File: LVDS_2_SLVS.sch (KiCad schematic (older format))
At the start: 6 parts

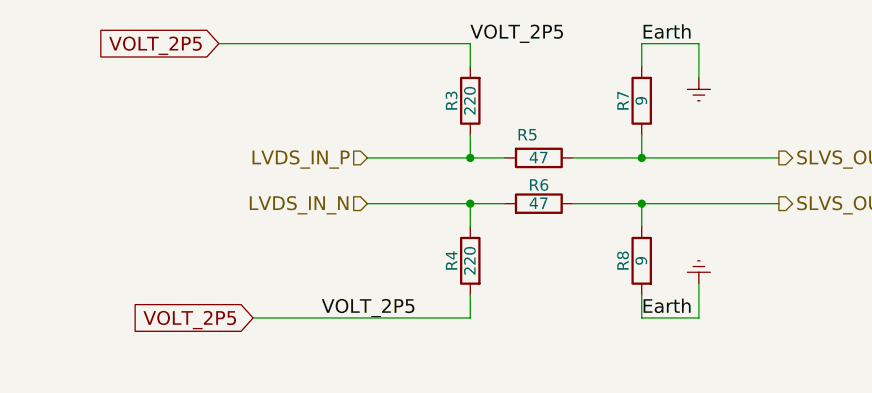
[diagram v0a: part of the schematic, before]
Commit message: Good, before replacing the swithches to TI ones
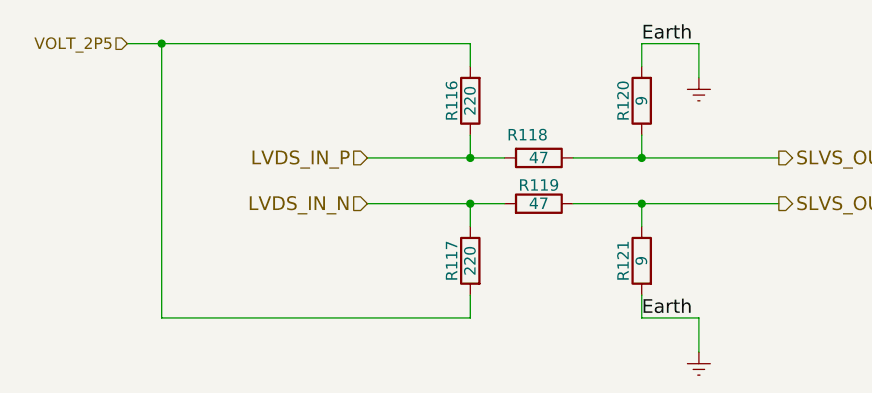
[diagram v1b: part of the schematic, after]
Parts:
- renumbered R6 to R100, R7 to R101, R8 to R102, R3 to R97, R4 to R98, R5 to R99

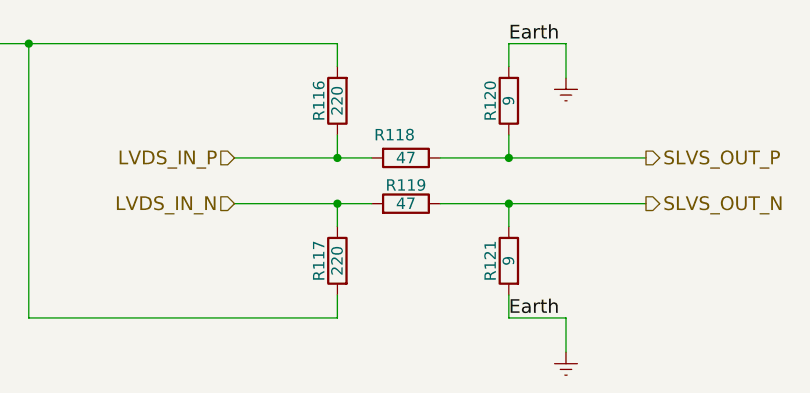
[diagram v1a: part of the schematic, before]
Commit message: good, added re-driver
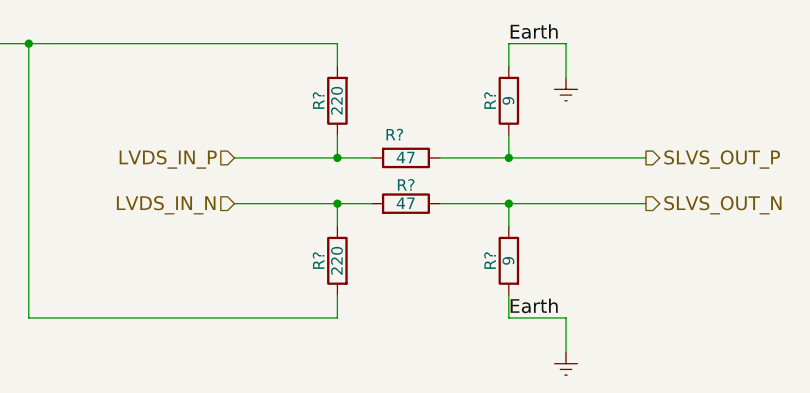
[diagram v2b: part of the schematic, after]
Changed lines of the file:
@@
 $Descr A4 11693 8268
 encoding utf-8
-Sheet 31 32
+Sheet 31 20
 Title ""
 Date ""
@@
 AR Path="/6191D89C/61A38142/61C10965/61958BD7/5955E861" Ref="R?"  Part="1"
 AR Path="/6191D89C/61A38142/61C10965/61946DF5/5955E861" Ref="R?"  Part="1"
-F 0 "R116" V 2680 1250 50  0000 C CNN
+AR Path="/6191D89C/61A814B9/61AF86EB/5955E861" Ref="R?"  Part="1"
+AR Path="/6191D89C/61A814B9/61AF8785/5955E861" Ref="R?"  Part="1"
+AR Path="/6191D89C/61A814B9/61AF878C/5955E861" Ref="R?"  Part="1"
+AR Path="/6191D89C/61A38142/61AF86EB/5955E861" Ref="R?"  Part="1"
+AR Path="/6191D89C/61A38142/61AF8785/5955E861" Ref="R?"  Part="1"
+AR Path="/6191D89C/61A38142/61AF878C/5955E861" Ref="R?"  Part="1"
+F 0 "R?" V 2680 1250 50  0000 C CNN
 F 1 "220" V 2600 1250 50  0000 C CNN
 F 2 "Resistors_SMD:R_0805" V 2530 1250 50  0001 C CNN
@@
 AR Path="/6191D89C/61A38142/61C10965/61958BD7/5955E8CA" Ref="R?"  Part="1"
 AR Path="/6191D89C/61A38142/61C10965/61946DF5/5955E8CA" Ref="R?"  Part="1"
-F 0 "R118" V 2800 1450 50  0000 C CNN
+AR Path="/6191D89C/61A814B9/61AF86EB/5955E8CA" Ref="R?"  Part="1"
+AR Path="/6191D89C/61A814B9/61AF8785/5955E8CA" Ref="R?"  Part="1"
+AR Path="/6191D89C/61A814B9/61AF878C/5955E8CA" Ref="R?"  Part="1"
+AR Path="/6191D89C/61A38142/61AF86EB/5955E8CA" Ref="R?"  Part="1"
+AR Path="/6191D89C/61A38142/61AF8785/5955E8CA" Ref="R?"  Part="1"
+AR Path="/6191D89C/61A38142/61AF878C/5955E8CA" Ref="R?"  Part="1"
+F 0 "R?" V 2800 1450 50  0000 C CNN
 F 1 "47" V 2900 1500 50  0000 C CNN
 F 2 "Resistors_SMD:R_0805" V 2830 1500 50  0001 C CNN
@@
 AR Path="/6191D89C/61A38142/61C10965/61958BD7/5955E920" Ref="R?"  Part="1"
 AR Path="/6191D89C/61A38142/61C10965/61946DF5/5955E920" Ref="R?"  Part="1"
-F 0 "R120" V 3430 1250 50  0000 C CNN
+AR Path="/6191D89C/61A814B9/61AF86EB/5955E920" Ref="R?"  Part="1"
+AR Path="/6191D89C/61A814B9/61AF8785/5955E920" Ref="R?"  Part="1"
+AR Path="/6191D89C/61A814B9/61AF878C/5955E920" Ref="R?"  Part="1"
+AR Path="/6191D89C/61A38142/61AF86EB/5955E920" Ref="R?"  Part="1"
+AR Path="/6191D89C/61A38142/61AF8785/5955E920" Ref="R?"  Part="1"
+AR Path="/6191D89C/61A38142/61AF878C/5955E920" Ref="R?"  Part="1"
+F 0 "R?" V 3430 1250 50  0000 C CNN
 F 1 "9" V 3350 1250 50  0000 C CNN
 F 2 "Resistors_SMD:R_0805" V 3280 1250 50  0001 C CNN
@@
 AR Path="/6191D89C/61A38142/61C10965/61958BD7/5955F5BB" Ref="R?"  Part="1"
 AR Path="/6191D89C/61A38142/61C10965/61946DF5/5955F5BB" Ref="R?"  Part="1"
-F 0 "R117" V 2680 1950 50  0000 C CNN
+AR Path="/6191D89C/61A814B9/61AF86EB/5955F5BB" Ref="R?"  Part="1"
+AR Path="/6191D89C/61A814B9/61AF8785/5955F5BB" Ref="R?"  Part="1"
+AR Path="/6191D89C/61A814B9/61AF878C/5955F5BB" Ref="R?"  Part="1"
+AR Path="/6191D89C/61A38142/61AF86EB/5955F5BB" Ref="R?"  Part="1"
+AR Path="/6191D89C/61A38142/61AF8785/5955F5BB" Ref="R?"  Part="1"
+AR Path="/6191D89C/61A38142/61AF878C/5955F5BB" Ref="R?"  Part="1"
+F 0 "R?" V 2680 1950 50  0000 C CNN
 F 1 "220" V 2600 1950 50  0000 C CNN
 F 2 "Resistors_SMD:R_0805" V 2530 1950 50  0001 C CNN
@@
 AR Path="/6191D89C/61A38142/61C10965/61958BD7/5955F5C4" Ref="R?"  Part="1"
 AR Path="/6191D89C/61A38142/61C10965/61946DF5/5955F5C4" Ref="R?"  Part="1"
-F 0 "R119" V 2980 1700 50  0000 C CNN
+AR Path="/6191D89C/61A814B9/61AF86EB/5955F5C4" Ref="R?"  Part="1"
+AR Path="/6191D89C/61A814B9/61AF8785/5955F5C4" Ref="R?"  Part="1"
+AR Path="/6191D89C/61A814B9/61AF878C/5955F5C4" Ref="R?"  Part="1"
+AR Path="/6191D89C/61A38142/61AF86EB/5955F5C4" Ref="R?"  Part="1"
+AR Path="/6191D89C/61A38142/61AF8785/5955F5C4" Ref="R?"  Part="1"
+AR Path="/6191D89C/61A38142/61AF878C/5955F5C4" Ref="R?"  Part="1"
+F 0 "R?" V 2980 1700 50  0000 C CNN
 F 1 "47" V 2900 1700 50  0000 C CNN
 F 2 "Resistors_SMD:R_0805" V 2830 1700 50  0001 C CNN
@@
 AR Path="/6191D89C/61A38142/61C10965/61958BD7/5955F5CD" Ref="R?"  Part="1"
 AR Path="/6191D89C/61A38142/61C10965/61946DF5/5955F5CD" Ref="R?"  Part="1"
-F 0 "R121" V 3430 1950 50  0000 C CNN
+AR Path="/6191D89C/61A814B9/61AF86EB/5955F5CD" Ref="R?"  Part="1"
+AR Path="/6191D89C/61A814B9/61AF8785/5955F5CD" Ref="R?"  Part="1"
+AR Path="/6191D89C/61A814B9/61AF878C/5955F5CD" Ref="R?"  Part="1"
+AR Path="/6191D89C/61A38142/61AF86EB/5955F5CD" Ref="R?"  Part="1"
+AR Path="/6191D89C/61A38142/61AF8785/5955F5CD" Ref="R?"  Part="1"
+AR Path="/6191D89C/61A38142/61AF878C/5955F5CD" Ref="R?"  Part="1"
+F 0 "R?" V 3430 1950 50  0000 C CNN
 F 1 "9" V 3350 1950 50  0000 C CNN
 F 2 "Resistors_SMD:R_0805" V 3280 1950 50  0001 C CNN
@@
 AR Path="/6191D89C/61A38142/61C10965/61958BD7/5955F5D7" Ref="#PWR?"  Part="1"
 AR Path="/6191D89C/61A38142/61C10965/61946DF5/5955F5D7" Ref="#PWR?"  Part="1"
-F 0 "#PWR077" H 3600 2100 50  0001 C CNN
+AR Path="/6191D89C/61A814B9/61AF86EB/5955F5D7" Ref="#PWR?"  Part="1"
+AR Path="/6191D89C/61A814B9/61AF8785/5955F5D7" Ref="#PWR?"  Part="1"
+AR Path="/6191D89C/61A814B9/61AF878C/5955F5D7" Ref="#PWR?"  Part="1"
+AR Path="/6191D89C/61A38142/61AF86EB/5955F5D7" Ref="#PWR?"  Part="1"
+AR Path="/6191D89C/61A38142/61AF8785/5955F5D7" Ref="#PWR?"  Part="1"
+AR Path="/6191D89C/61A38142/61AF878C/5955F5D7" Ref="#PWR?"  Part="1"
+F 0 "#PWR?" H 3600 2100 50  0001 C CNN
 F 1 "Earth" H 3600 2200 50  0001 C CNN
 F 2 "" H 3600 2350 50  0000 C CNN
@@
 AR Path="/6191D89C/61A38142/61C10965/61958BD7/5955F488" Ref="#PWR?"  Part="1"
 AR Path="/6191D89C/61A38142/61C10965/61946DF5/5955F488" Ref="#PWR?"  Part="1"
-F 0 "#PWR076" H 3600 900 50  0001 C CNN
+AR Path="/6191D89C/61A814B9/61AF86EB/5955F488" Ref="#PWR?"  Part="1"
+AR Path="/6191D89C/61A814B9/61AF8785/5955F488" Ref="#PWR?"  Part="1"
+AR Path="/6191D89C/61A814B9/61AF878C/5955F488" Ref="#PWR?"  Part="1"
+AR Path="/6191D89C/61A38142/61AF86EB/5955F488" Ref="#PWR?"  Part="1"
+AR Path="/6191D89C/61A38142/61AF8785/5955F488" Ref="#PWR?"  Part="1"
+AR Path="/6191D89C/61A38142/61AF878C/5955F488" Ref="#PWR?"  Part="1"
+F 0 "#PWR?" H 3600 900 50  0001 C CNN
 F 1 "Earth" H 3600 1000 50  0001 C CNN
 F 2 "" H 3600 1150 50  0000 C CNN

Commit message: good, before reducing
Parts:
- R101, R102: value 9 -> 12
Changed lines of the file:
@@
 $Descr A4 11693 8268
 encoding utf-8
-Sheet 31 20
+Sheet 7 15
 Title ""
 Date ""
@@
 AR Path="/6191D89C/61A38142/61AF8785/5955E861" Ref="R?"  Part="1"
 AR Path="/6191D89C/61A38142/61AF878C/5955E861" Ref="R?"  Part="1"
-F 0 "R?" V 2680 1250 50  0000 C CNN
+AR Path="/6191D89C/61A814B9/61B2E698/61C84312/5955E861" Ref="R21"  Part="1"
+AR Path="/6191D89C/61A814B9/61B8C8BE/61C84312/5955E861" Ref="R45"  Part="1"
+AR Path="/6191D89C/61A814B9/61B2E698/61CC513F/5955E861" Ref="R27"  Part="1"
+AR Path="/6191D89C/61A814B9/61B8C8BE/61CC513F/5955E861" Ref="R51"  Part="1"
+AR Path="/6191D89C/61A814B9/61B2E698/61CC9F81/5955E861" Ref="R33"  Part="1"
+AR Path="/6191D89C/61A814B9/61B8C8BE/61CC9F81/5955E861" Ref="R57"  Part="1"
+AR Path="/6191D89C/61A814B9/61B2E698/61CCEEAC/5955E861" Ref="R39"  Part="1"
+AR Path="/6191D89C/61A814B9/61B8C8BE/61CCEEAC/5955E861" Ref="R63"  Part="1"
+F 0 "R21" V 2680 1250 50  0000 C CNN
 F 1 "220" V 2600 1250 50  0000 C CNN
 F 2 "Resistors_SMD:R_0805" V 2530 1250 50  0001 C CNN
@@
 AR Path="/6191D89C/61A38142/61AF8785/5955E8CA" Ref="R?"  Part="1"
 AR Path="/6191D89C/61A38142/61AF878C/5955E8CA" Ref="R?"  Part="1"
-F 0 "R?" V 2800 1450 50  0000 C CNN
+AR Path="/6191D89C/61A814B9/61B2E698/61C84312/5955E8CA" Ref="R23"  Part="1"
+AR Path="/6191D89C/61A814B9/61B8C8BE/61C84312/5955E8CA" Ref="R47"  Part="1"
+AR Path="/6191D89C/61A814B9/61B2E698/61CC513F/5955E8CA" Ref="R29"  Part="1"
+AR Path="/6191D89C/61A814B9/61B8C8BE/61CC513F/5955E8CA" Ref="R53"  Part="1"
+AR Path="/6191D89C/61A814B9/61B2E698/61CC9F81/5955E8CA" Ref="R35"  Part="1"
+AR Path="/6191D89C/61A814B9/61B8C8BE/61CC9F81/5955E8CA" Ref="R59"  Part="1"
+AR Path="/6191D89C/61A814B9/61B2E698/61CCEEAC/5955E8CA" Ref="R41"  Part="1"
+AR Path="/6191D89C/61A814B9/61B8C8BE/61CCEEAC/5955E8CA" Ref="R65"  Part="1"
+F 0 "R23" V 2800 1450 50  0000 C CNN
 F 1 "47" V 2900 1500 50  0000 C CNN
 F 2 "Resistors_SMD:R_0805" V 2830 1500 50  0001 C CNN
@@
 AR Path="/6191D89C/61A38142/61AF8785/5955E920" Ref="R?"  Part="1"
 AR Path="/6191D89C/61A38142/61AF878C/5955E920" Ref="R?"  Part="1"
-F 0 "R?" V 3430 1250 50  0000 C CNN
-F 1 "9" V 3350 1250 50  0000 C CNN
+AR Path="/6191D89C/61A814B9/61B2E698/61C84312/5955E920" Ref="R25"  Part="1"
+AR Path="/6191D89C/61A814B9/61B8C8BE/61C84312/5955E920" Ref="R49"  Part="1"
+AR Path="/6191D89C/61A814B9/61B2E698/61CC513F/5955E920" Ref="R31"  Part="1"
+AR Path="/6191D89C/61A814B9/61B8C8BE/61CC513F/5955E920" Ref="R55"  Part="1"
+AR Path="/6191D89C/61A814B9/61B2E698/61CC9F81/5955E920" Ref="R37"  Part="1"
+AR Path="/6191D89C/61A814B9/61B8C8BE/61CC9F81/5955E920" Ref="R61"  Part="1"
+AR Path="/6191D89C/61A814B9/61B2E698/61CCEEAC/5955E920" Ref="R43"  Part="1"
+AR Path="/6191D89C/61A814B9/61B8C8BE/61CCEEAC/5955E920" Ref="R67"  Part="1"
+F 0 "R25" V 3430 1250 50  0000 C CNN
+F 1 "12" V 3350 1250 50  0000 C CNN
 F 2 "Resistors_SMD:R_0805" V 3280 1250 50  0001 C CNN
 F 3 "http://eu.mouser.com/ProductDetail/Yageo/RC0805FR-0712RL/?qs=sGAEpiMZZMu61qfTUdNhG%252bqOb1cAxvLka%2fP6Zd2mQhw%3d" H 3350 1250 50  0001 C CNN
@@
 AR Path="/6191D89C/61A38142/61AF8785/5955F5BB" Ref="R?"  Part="1"
 AR Path="/6191D89C/61A38142/61AF878C/5955F5BB" Ref="R?"  Part="1"
-F 0 "R?" V 2680 1950 50  0000 C CNN
+AR Path="/6191D89C/61A814B9/61B2E698/61C84312/5955F5BB" Ref="R22"  Part="1"
+AR Path="/6191D89C/61A814B9/61B8C8BE/61C84312/5955F5BB" Ref="R46"  Part="1"
+AR Path="/6191D89C/61A814B9/61B2E698/61CC513F/5955F5BB" Ref="R28"  Part="1"
+AR Path="/6191D89C/61A814B9/61B8C8BE/61CC513F/5955F5BB" Ref="R52"  Part="1"
+AR Path="/6191D89C/61A814B9/61B2E698/61CC9F81/5955F5BB" Ref="R34"  Part="1"
+AR Path="/6191D89C/61A814B9/61B8C8BE/61CC9F81/5955F5BB" Ref="R58"  Part="1"
+AR Path="/6191D89C/61A814B9/61B2E698/61CCEEAC/5955F5BB" Ref="R40"  Part="1"
+AR Path="/6191D89C/61A814B9/61B8C8BE/61CCEEAC/5955F5BB" Ref="R64"  Part="1"
+F 0 "R22" V 2680 1950 50  0000 C CNN
 F 1 "220" V 2600 1950 50  0000 C CNN
 F 2 "Resistors_SMD:R_0805" V 2530 1950 50  0001 C CNN
@@
 AR Path="/6191D89C/61A38142/61AF8785/5955F5C4" Ref="R?"  Part="1"
 AR Path="/6191D89C/61A38142/61AF878C/5955F5C4" Ref="R?"  Part="1"
-F 0 "R?" V 2980 1700 50  0000 C CNN
+AR Path="/6191D89C/61A814B9/61B2E698/61C84312/5955F5C4" Ref="R24"  Part="1"
+AR Path="/6191D89C/61A814B9/61B8C8BE/61C84312/5955F5C4" Ref="R48"  Part="1"
+AR Path="/6191D89C/61A814B9/61B2E698/61CC513F/5955F5C4" Ref="R30"  Part="1"
+AR Path="/6191D89C/61A814B9/61B8C8BE/61CC513F/5955F5C4" Ref="R54"  Part="1"
+AR Path="/6191D89C/61A814B9/61B2E698/61CC9F81/5955F5C4" Ref="R36"  Part="1"
+AR Path="/6191D89C/61A814B9/61B8C8BE/61CC9F81/5955F5C4" Ref="R60"  Part="1"
+AR Path="/6191D89C/61A814B9/61B2E698/61CCEEAC/5955F5C4" Ref="R42"  Part="1"
+AR Path="/6191D89C/61A814B9/61B8C8BE/61CCEEAC/5955F5C4" Ref="R66"  Part="1"
+F 0 "R24" V 2980 1700 50  0000 C CNN
 F 1 "47" V 2900 1700 50  0000 C CNN
 F 2 "Resistors_SMD:R_0805" V 2830 1700 50  0001 C CNN
@@
 AR Path="/6191D89C/61A38142/61AF8785/5955F5CD" Ref="R?"  Part="1"
 AR Path="/6191D89C/61A38142/61AF878C/5955F5CD" Ref="R?"  Part="1"
-F 0 "R?" V 3430 1950 50  0000 C CNN
-F 1 "9" V 3350 1950 50  0000 C CNN
+AR Path="/6191D89C/61A814B9/61B2E698/61C84312/5955F5CD" Ref="R26"  Part="1"
+AR Path="/6191D89C/61A814B9/61B8C8BE/61C84312/5955F5CD" Ref="R50"  Part="1"
+AR Path="/6191D89C/61A814B9/61B2E698/61CC513F/5955F5CD" Ref="R32"  Part="1"
+AR Path="/6191D89C/61A814B9/61B8C8BE/61CC513F/5955F5CD" Ref="R56"  Part="1"
+AR Path="/6191D89C/61A814B9/61B2E698/61CC9F81/5955F5CD" Ref="R38"  Part="1"
+AR Path="/6191D89C/61A814B9/61B8C8BE/61CC9F81/5955F5CD" Ref="R62"  Part="1"
+AR Path="/6191D89C/61A814B9/61B2E698/61CCEEAC/5955F5CD" Ref="R44"  Part="1"
+AR Path="/6191D89C/61A814B9/61B8C8BE/61CCEEAC/5955F5CD" Ref="R68"  Part="1"
+F 0 "R26" V 3430 1950 50  0000 C CNN
+F 1 "12" V 3350 1950 50  0000 C CNN
 F 2 "Resistors_SMD:R_0805" V 3280 1950 50  0001 C CNN
 F 3 "http://eu.mouser.com/ProductDetail/Yageo/RC0805FR-0712RL/?qs=sGAEpiMZZMu61qfTUdNhG%252bqOb1cAxvLka%2fP6Zd2mQhw%3d" H 3350 1950 50  0001 C CNN
@@
 AR Path="/6191D89C/61A38142/61AF8785/5955F5D7" Ref="#PWR?"  Part="1"
 AR Path="/6191D89C/61A38142/61AF878C/5955F5D7" Ref="#PWR?"  Part="1"
-F 0 "#PWR?" H 3600 2100 50  0001 C CNN
+AR Path="/6191D89C/61A814B9/61B2E698/61C84312/5955F5D7" Ref="#PWR0107"  Part="1"
+AR Path="/6191D89C/61A814B9/61B8C8BE/61C84312/5955F5D7" Ref="#PWR0115"  Part="1"
+AR Path="/6191D89C/61A814B9/61B2E698/61CC513F/5955F5D7" Ref="#PWR0109"  Part="1"
+AR Path="/6191D89C/61A814B9/61B8C8BE/61CC513F/5955F5D7" Ref="#PWR0117"  Part="1"
+AR Path="/6191D89C/61A814B9/61B2E698/61CC9F81/5955F5D7" Ref="#PWR0111"  Part="1"
+AR Path="/6191D89C/61A814B9/61B8C8BE/61CC9F81/5955F5D7" Ref="#PWR0119"  Part="1"
+AR Path="/6191D89C/61A814B9/61B2E698/61CCEEAC/5955F5D7" Ref="#PWR0113"  Part="1"
+AR Path="/6191D89C/61A814B9/61B8C8BE/61CCEEAC/5955F5D7" Ref="#PWR0121"  Part="1"
+F 0 "#PWR0107" H 3600 2100 50  0001 C CNN
 F 1 "Earth" H 3600 2200 50  0001 C CNN
 F 2 "" H 3600 2350 50  0000 C CNN
@@
 AR Path="/6191D89C/61A38142/61AF8785/5955F488" Ref="#PWR?"  Part="1"
 AR Path="/6191D89C/61A38142/61AF878C/5955F488" Ref="#PWR?"  Part="1"
-F 0 "#PWR?" H 3600 900 50  0001 C CNN
+AR Path="/6191D89C/61A814B9/61B2E698/61C84312/5955F488" Ref="#PWR0108"  Part="1"
+AR Path="/6191D89C/61A814B9/61B8C8BE/61C84312/5955F488" Ref="#PWR0116"  Part="1"
+AR Path="/6191D89C/61A814B9/61B2E698/61CC513F/5955F488" Ref="#PWR0110"  Part="1"
+AR Path="/6191D89C/61A814B9/61B8C8BE/61CC513F/5955F488" Ref="#PWR0118"  Part="1"
+AR Path="/6191D89C/61A814B9/61B2E698/61CC9F81/5955F488" Ref="#PWR0112"  Part="1"
+AR Path="/6191D89C/61A814B9/61B8C8BE/61CC9F81/5955F488" Ref="#PWR0120"  Part="1"
+AR Path="/6191D89C/61A814B9/61B2E698/61CCEEAC/5955F488" Ref="#PWR0114"  Part="1"
+AR Path="/6191D89C/61A814B9/61B8C8BE/61CCEEAC/5955F488" Ref="#PWR0122"  Part="1"
+F 0 "#PWR0108" H 3600 900 50  0001 C CNN
 F 1 "Earth" H 3600 1000 50  0001 C CNN
 F 2 "" H 3600 1150 50  0000 C CNN

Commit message: before re-arranging
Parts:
- removed R98: 220, Resistors_SMD:R_0805, symbol Device:R
- removed R99: 47, Resistors_SMD:R_0805, symbol Device:R
- added R13: 220, Resistors_SMD:R_0603, symbol Device:R
- added R14: 47, Resistors_SMD:R_0603, symbol Device:R
- R12: renamed from R97; footprint Resistors_SMD:R_0805 -> Resistors_SMD:R_0603; Part Number RC0805FR-07220RL -> RC0603FR-07220RL; Power 1/8W -> 100mW
- R15: renamed from R100; footprint Resistors_SMD:R_0805 -> Resistors_SMD:R_0603; Part Number RC0805FR-0747RL -> RC0603FR-0747RL; Power 1/8W -> 100 mW
- renumbered R101 to R16, R102 to R17
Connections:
- net LVDS_IN_N: now also R13.2
- net LVDS_IN_P: now also R14.2
- net SLVS_OUT_P: now also R14.1
- net VOLT_2P5: now also R13.1

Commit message: rev 2022
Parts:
- R16, R17: value 12 -> 9.1; footprint Resistors_SMD:R_0805 -> Resistors_SMD:R_0603_HandSoldering; Part Number RC0805FR-0712RL -> (none); Power 1/8W -> 250 mW
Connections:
- net Earth: now also R17.1; no longer R17.2
- net SLVS_OUT_N: now also R17.2; no longer R17.1

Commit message: minor changes 4
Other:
- note added: "NOTE: Every such block consumes around 20mA.\n\nFor 18 blocks (Six (6) 2 lanes CSI + 6 clocks) = 6*2 + 6 = 18 we need 18*0.02A = 0.36 A ,around 0.5 A"
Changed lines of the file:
@@
 $Descr A4 11693 8268
 encoding utf-8
-Sheet 11 10
+Sheet 10 11
 Title ""
 Date ""
@@
 	-1   0    0    1
 $EndComp
+Text Notes 1100 3000 0    79   ~ 16
+NOTE: Every such block consumes around 20mA.\n\nFor 18 blocks (Six (6) 2 lanes CSI + 6 clocks) = 6*2 + 6 = 18 we need 18*0.02A = 0.36 A ,around 0.5 A
 $EndSCHEMATC
